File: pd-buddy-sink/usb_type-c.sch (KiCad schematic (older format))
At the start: 1 part, among them J2 USB_C_Receptacle

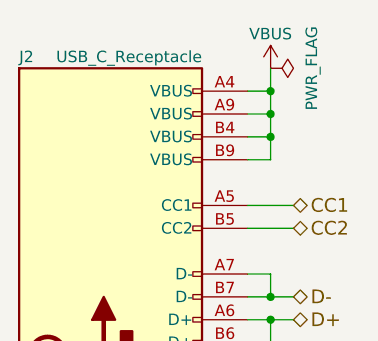
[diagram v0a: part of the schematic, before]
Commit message: Use USB connector from Connectors_USB.pretty
My USB Type-C connectors were merged into the KiCad
Connectors_USB.pretty footprint library, so I can use it from the normal
library now.
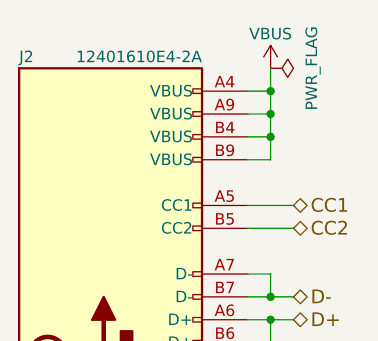
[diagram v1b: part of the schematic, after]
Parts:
- J2: value USB_C_Receptacle -> 12401610E4-2A; footprint pd-buddy:Amphenol-12401610E4#2A -> Connectors_USB:USB_C_Receptacle_Amphenol_12401610E4-2A
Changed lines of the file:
@@
 P 6000 3150
 F 0 "J2" H 5600 4600 50  0000 L CNN
-F 1 "USB_C_Receptacle" H 6400 4600 50  0000 R CNN
-F 2 "pd-buddy:Amphenol-12401610E4#2A" H 6150 3150 50  0001 C CNN
-F 3 "" H 6150 3150 50  0001 C CNN
+F 1 "12401610E4-2A" H 6400 4600 50  0000 R CNN
+F 2 "Connectors_USB:USB_C_Receptacle_Amphenol_12401610E4-2A" H 6150 3150 50  0001 C CNN
+F 3 "https://www.amphenolcanada.com/StockAvailabilityPrice.aspx?From=&PartNum=12401610E4%7e2A" H 6150 3150 50  0001 C CNN
 	1    6000 3150
 	1    0    0    -1
@@
 Connection ~ 6700 1850
 $Comp
-L PWR_FLAG #FLG1
+L PWR_FLAG #FLG035
 U 1 1 591479A3
 P 6700 1750
-F 0 "#FLG1" H 6700 1845 50  0001 C CNN
+F 0 "#FLG035" H 6700 1845 50  0001 C CNN
 F 1 "PWR_FLAG" H 6700 1930 50  0000 C CNN
 F 2 "" H 6700 1750 50  0000 C CNN
@@
 	6100 4750 6100 4950
 $Comp
-L GND #PWR36
+L GND #PWR036
 U 1 1 59147BA2
 P 6100 4950
-F 0 "#PWR36" H 6100 4700 50  0001 C CNN
+F 0 "#PWR036" H 6100 4700 50  0001 C CNN
 F 1 "GND" H 6100 4800 50  0000 C CNN
 F 2 "" H 6100 4950 50  0000 C CNN
@@
 $EndComp
 $Comp
-L PWR_FLAG #FLG2
+L PWR_FLAG #FLG037
 U 1 1 59147BB3
 P 6100 4950
-F 0 "#FLG2" H 6100 5045 50  0001 C CNN
+F 0 "#FLG037" H 6100 5045 50  0001 C CNN
 F 1 "PWR_FLAG" H 6100 5130 50  0000 C CNN
 F 2 "" H 6100 4950 50  0000 C CNN
@@
 Connection ~ 5800 4850
 $Comp
-L VBUS #PWR35
+L VBUS #PWR038
 U 1 1 592B5855
 P 6700 1750
-F 0 "#PWR35" H 6700 1600 50  0001 C CNN
+F 0 "#PWR038" H 6700 1600 50  0001 C CNN
 F 1 "VBUS" H 6700 1900 50  0000 C CNN
 F 2 "" H 6700 1750 50  0001 C CNN
